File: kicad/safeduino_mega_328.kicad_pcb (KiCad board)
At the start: 2 copper layers, 134.5 x 63.9 mm, 333 parts, among them X1 USB

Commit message: Начал переразводить печатную плату.
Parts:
- removed XSJG1: ~, SIL-4
- added C1: 22п, SMD0805, B.Cu at (68.6, 101.1)
- added C10: 0.1мк, SMD0805, B.Cu at (107.8, 133.0)
- added C8: 0.1мк, SMD0805, B.Cu at (72.3, 119.0)
- added C9: 0.1мк, SMD0805, F.Cu at (69.6, 121.2)
- added R10: 10к, SMD0805, B.Cu at (72.3, 115.1)
- added R11: 1M, SMD0805, B.Cu at (72.9, 101.1)
- added R12: 10к, SMD0805, F.Cu at (82.5, 119.3)
- added R13: 10к, SMD0805, F.Cu at (82.5, 113.5)
- added R14: 1к, SMD0805, B.Cu at (105.5, 133.9)
- added R15: 0, SMD0805, B.Cu at (104.6, 130.8)
- added R16: 1М, SMD0805, B.Cu at (110.1, 133.0)
- added R9: 1к, SMD0805, F.Cu at (58.8, 120.4)
- added VD5: BAS216, SOD110, B.Cu at (69.8, 113.9)
- added XP1: PLD-6, PIN_ARRAY_3x2, F.Cu at (85.1, 104.6)
- added Z2: 16МГц, Q_49U3HMS&, F.Cu at (72.9, 104.5)
- C3: value 0.1мк -> 22п; moved to B.Cu
- C4: moved to B.Cu
- C5: value 0.1мк -> 1мк; moved to B.Cu
- DD2: value FT232RL -> ATMEGA16U2-MU; footprint TSOP28 -> TQFP32_case
- DD3: value ADUM1201 -> ADUM1301; footprint SOIC8 -> SOIC16_RW16
- R3: value 47 -> 22
- R4: value 1к -> 22
- XP2: footprint pin_array_3x2 -> PIN_ARRAY_3x2
- XS1, XS3, XS5, XS6: footprint SIL-8 -> PIN_ARRAY_8x1
- XS2, XS4: footprint SIL-6 -> PIN_ARRAY_6x1
- moved VD4 26.5 mm to (64.1, 120.8), turned to 0 degrees
- moved C5 22.7 mm to (66.3, 114.4)
- moved R4 19.2 mm to (66.2, 110.9), turned to 0 degrees
- moved C2 19.0 mm to (77.5, 128.1), turned to 0 degrees
- moved R3 18.7 mm to (66.2, 108.6)
- moved VD3 17.6 mm to (64.1, 117.9)
- moved C3 11.4 mm to (77.2, 101.1), turned to 0 degrees
- moved R2 11.0 mm to (65.7, 114.3), turned to 90 degrees
- moved C4 8.77 mm to (74.2, 120.5), turned to 0 degrees
- moved C12 7.39 mm to (82.0, 110.4), turned to 0 degrees
- moved DD2 5.53 mm to (74.7, 115.6)
- moved C6 2.44 mm to (75.9, 124.6), turned to 0 degrees
- moved R7 2.08 mm to (98.3, 115.2)
- moved C13 1.73 mm to (93.5, 108.3), turned to 180 degrees
- moved DA1 1.52 mm to (85.5, 123.8)
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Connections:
- C3 pad 1: N-0000013 -> N-0000060
- C4 pad 1: /5V_USB -> /GND_USB
- C4 pad 2: /GND_USB -> /5V_USB
- C5 pad 1: /GND_USB -> N-0000065
- C5 pad 2: /5V_USB -> /GND_USB
- DD2 pad 1: N-0000026 -> N-000003
- DD2 pad 10: /DCD -> /RXI
- DD2 pad 11: /CTS -> /TXI
- DD2 pad 13: (no net) -> /RESET2
- DD2 pad 15: N-0000061 -> /SCK2
- DD2 pad 16: N-0000060 -> /MOSI2
- DD2 pad 17: N-0000013 -> /MISO2
- DD2 pad 18: /GND_USB -> (no net)
- DD2 pad 19: /5V_USB -> (no net)
- DD2 pad 2: (no net) -> N-0000060
- DD2 pad 20: /5V_USB -> (no net)
- DD2 pad 21: /GND_USB -> (no net)
- DD2 pad 22: N-0000032 -> (no net)
- DD2 pad 23: N-0000036 -> (no net)
- DD2 pad 24: (no net) -> /RESET_16U2
- DD2 pad 25: /GND_USB -> (no net)
- DD2 pad 26: /GND_USB -> (no net)
- DD2 pad 27: (no net) -> N-0000065
- DD2 pad 28: (no net) -> /GND_USB
- DD2 pad 3: (no net) -> /GND_USB
- DD2 pad 5: N-0000038 -> (no net)
- DD2 pad 6: /RI -> (no net)
- DD2 pad 7: /GND_USB -> (no net)
- DD2 pad 9: /DSR -> /PE0
- DD3 pad 2: N-0000038 -> /GND_USB
- DD3 pad 3: N-0000064 -> /RESET2
- DD3 pad 4: /GND_USB -> N-0000047
- DD3 pad 5: /GND -> (no net)
- DD3 pad 6: N-0000047 -> (no net)
- DD3 pad 7: N-0000048 -> (no net)
- DD3 pad 8: /MPU_VCC -> /GND_USB
- R3 pad 1: N-0000026 -> N-0000034
- R3 pad 2: N-0000064 -> /D-
- R4 pad 1: N-0000057 -> N-0000058
- R4 pad 2: /5V_USB -> /D+
- R6 pad 1: N-0000047 -> N-0000045
- R7 pad 1: N-0000048 -> N-0000043
- VD3 pad 2: N-0000032 -> /RXI
- VD4 pad 2: N-0000036 -> /TXI
- X1 pad 2: N-0000060 -> N-0000034
- X1 pad 3: N-0000061 -> N-0000058
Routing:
- net /5V_USB: track 99.2 -> 2.81 mm, vias 2 -> 0
- net N-0000011: track 0.00 -> 26.5 mm, vias 0 -> 1
- net /DSR: track 25.6 -> 0.00 mm, vias 1 -> 0
- net /CTS: track 25.1 -> 0.00 mm, vias 1 -> 0
- net /MPU_VCC: track 297.0 -> 319.2 mm
- net /GND_USB: track 26.2 -> 6.25 mm, vias 9 -> 0
- net /RESET_16U2: track 0.00 -> 19.2 mm
- net /DCD: track 19.1 -> 0.00 mm, vias 1 -> 0
- net /MOSI2: track 0.00 -> 16.6 mm, vias 0 -> 1
- net N-0000036: track 15.7 -> 0.00 mm
- net /SCK2: track 0.00 -> 15.6 mm, vias 0 -> 1
- net /RI: track 14.4 -> 0.00 mm, vias 1 -> 0
- net N-0000061: track 13.5 -> 0.00 mm
- net N-0000032: track 11.4 -> 0.00 mm
- net N-0000038: track 9.76 -> 0.00 mm
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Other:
- board text removed: "CTS"
- board text removed: "DCD"
- board text removed: "DSR"
- board text removed: "RI"

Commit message: Закончил разводку платы.
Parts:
- C9: moved to B.Cu
- moved C8 7.81 mm to (64.5, 118.0), turned to 180 degrees
- moved R10 7.47 mm to (67.9, 109.0)
- moved VD5 7.19 mm to (65.7, 108.1)
- moved C4 4.70 mm to (77.9, 123.4), turned to 180 degrees
- moved C9 1.67 mm to (69.8, 122.8)
- moved C2 0.97 mm to (77.9, 127.3), turned to 180 degrees
- moved C6 0.57 mm to (75.7, 124.1), turned to 180 degrees
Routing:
- net /5V_USB: track 2.81 -> 105.5 mm, vias 0 -> 3
- net /GND_USB: track 6.25 -> 60.2 mm, vias 0 -> 5
- net N-000003: track 6.18 -> 27.1 mm, vias 0 -> 1
- net /TXI: track 0.00 -> 20.4 mm, vias 0 -> 2
- net N-0000060: track 6.18 -> 25.8 mm, vias 0 -> 1
- net /D-: track 0.00 -> 17.9 mm, vias 0 -> 2
- net /RXI: track 0.00 -> 14.7 mm, vias 0 -> 2
- net /D+: track 0.00 -> 13.3 mm, vias 0 -> 2
- net /RESET_16U2: track 19.2 -> 29.1 mm, vias 0 -> 1
- net N-0000065: track 0.00 -> 5.87 mm, vias 0 -> 1
- net /GND: track 134.9 -> 138.9 mm
- net /MOSI2: track 16.6 -> 13.6 mm
- net /SCK2: track 15.6 -> 14.2 mm

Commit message: Добавил самовостанавливающиеся предохренители на 0.5А.
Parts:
- added FU1: MF-MSMF050, SMD1812, B.Cu at (62.9, 103.9)
- added FU2: MF-MSMF050, SMD1812, B.Cu at (133.1, 140.1)
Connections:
- VD1 pad 1: N-0000031 -> N-0000057
- X1 pad 1: /5V_USB -> N-0000042
- XP3 pad 1: N-0000031 -> N-0000056
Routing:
- net N-0000042: track 0.00 -> 19.7 mm, vias 0 -> 1
- net N-0000056: track 0.00 -> 10.3 mm
- net N-0000057: track 0.00 -> 7.89 mm, vias 0 -> 1
- net N-0000031: track 6.36 -> 0.00 mm
- net /5V_USB: track 105.5 -> 108.2 mm, vias 3 -> 4

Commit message: Заменил резистор R15 на диод VD6  для защиты ADUM от попадания напряжения.
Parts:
- removed R15: 0, SMD0805
- added VD6: BAS216, SOD110, B.Cu at (103.1, 130.8)
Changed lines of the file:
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@@
     (thickness 1.6002)
     (drawings 81)
-    (tracks 943)
+    (tracks 944)
     (zones 0)
     (modules 349)
@@
   )
   (setup
-    (last_trace_width 0.508)
+    (last_trace_width 0.254)
     (user_trace_width 0.254)
     (user_trace_width 0.508)
@@
     )
   )
-  (module SMD0805 (layer Back)
-    (at 104.648 130.81)
-    (attr smd)
-    (fp_text reference R15 (at 0 -1.524) (layer B.SilkS)
-      (effects (font (size 0.635 0.635) (thickness 0.127)) (justify mirror))
-    )
-    (fp_text value 0 (at 0.254 -1.524) (layer B.SilkS) hide
-      (effects (font (size 0.635 0.635) (thickness 0.127)) (justify mirror))
-    )
-    (fp_line (start 1.778 -1.016) (end 1.778 1.016) (layer B.SilkS) (width 0.127))
-    (fp_line (start -1.778 -1.016) (end 1.778 -1.016) (layer B.SilkS) (width 0.127))
-    (fp_line (start -1.778 1.016) (end -1.778 -1.016) (layer B.SilkS) (width 0.127))
-    (fp_line (start -1.778 1.016) (end 1.778 1.016) (layer B.SilkS) (width 0.127))
-    (pad 1 smd rect (at -0.9525 0) (size 0.889 1.397)
-      (layers Back B.Paste B.Mask)
-      (net 40 N-0000013)
-    )
-    (pad 2 smd rect (at 0.9525 0) (size 0.889 1.397)
-      (layers Back B.Paste B.Mask)
-      (net 48 N-0000055)
-    )
-    (model smd/chip_cms.wrl
-      (at (xyz 0 0 0))
-      (scale (xyz 0.1 0.1 0.1))
-      (rotate (xyz 0 0 0))
-    )
-  )
   (module SMD0805 (layer Front)
     (at 82.042 110.363)
@@
     )
   )
+  (module SOD110 (layer Back)
+    (at 103.124 130.81)
+    (tags SOT23_5)
+    (fp_text reference VD6 (at 1.27 -1.778) (layer B.SilkS)
+      (effects (font (size 0.762 0.762) (thickness 0.0762)) (justify mirror))
+    )
+    (fp_text value BAS216 (at 1.397 -1.778) (layer B.SilkS) hide
+      (effects (font (size 0.762 0.50038) (thickness 0.0762)) (justify mirror))
+    )
+    (fp_line (start -0.889 -1.016) (end 3.556 -1.016) (layer B.SilkS) (width 0.127))
+    (fp_line (start 3.556 1.016) (end -0.889 1.016) (layer B.SilkS) (width 0.127))
+    (fp_line (start 3.556 1.016) (end 3.556 -1.016) (layer B.SilkS) (width 0.127))
+    (fp_line (start -0.889 -1.016) (end -0.889 1.016) (layer B.SilkS) (width 0.127))
+    (fp_line (start 3.302 1.016) (end 3.302 -1.016) (layer B.SilkS) (width 0.127))
+    (pad 2 smd rect (at 2.3495 0) (size 1.00076 1.19888)
+      (layers Back B.Paste B.Mask)
+      (net 48 N-0000055)
+    )
+    (pad 1 smd rect (at 0 0) (size 1.00076 1.19888)
+      (layers Back B.Paste B.Mask)
+      (net 40 N-0000013)
+    )
+    (model smd/SOT23_6.wrl
+      (at (xyz 0 0 0))
+      (scale (xyz 0.11 0.11 0.11))
+      (rotate (xyz 0 0 -180))
+    )
+  )
   (gr_text "SafeDuino MEGA 328 \nrev 1.02" (at 57.277 131.064 90) (layer F.SilkS)
     (effects (font (size 1.09982 1.09982) (thickness 0.17018)))
@@
   (segment (start 85.471 139.065) (end 78.105 139.065) (width 0.508) (layer Front) (net 39))
   (segment (start 78.105 139.065) (end 77.47 139.7) (width 0.508) (layer Front) (net 39))
-  (segment (start 103.6955 130.81) (end 101.6 130.81) (width 0.254) (layer Back) (net 40))
+  (segment (start 101.473 130.683) (end 102.997 130.683) (width 0.254) (layer Back) (net 40) (status 800000))
+  (segment (start 102.997 130.683) (end 103.124 130.81) (width 0.254) (layer Back) (net 40) (status C00000))
   (segment (start 94.107 113.411) (end 95.25 113.411) (width 0.254) (layer Front) (net 40))
   (segment (start 93.345 114.173) (end 94.107 113.411) (width 0.254) (layer Front) (net 40))

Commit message: SafeDuino MEGA 328 v1.02 полностью готова к отправке на изготовление.
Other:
- board text added: "+5V"

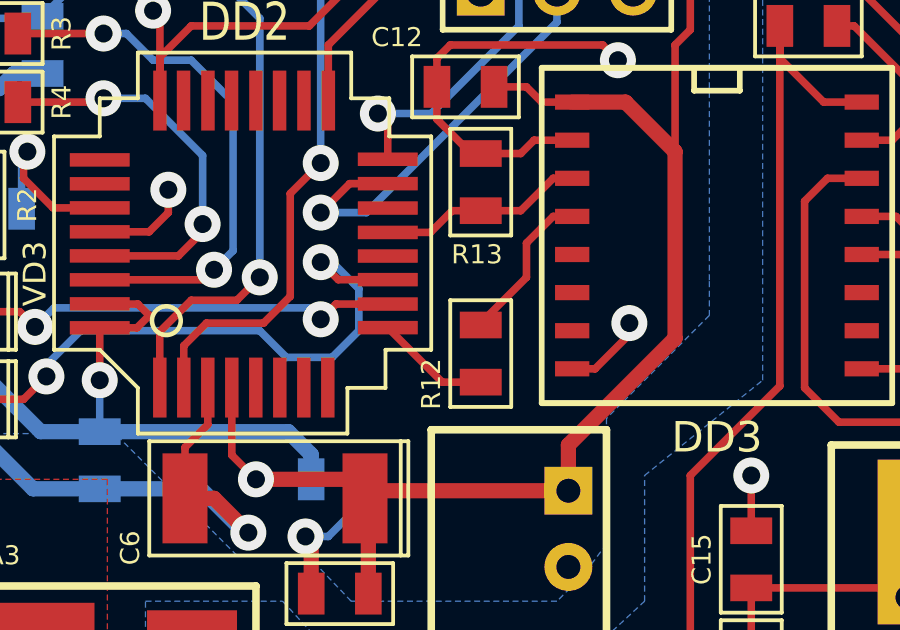
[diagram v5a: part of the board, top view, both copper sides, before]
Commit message: Исправли ошибку на плате SafeDuino MEGA 328(был не соединён контакт PE0 на плате).
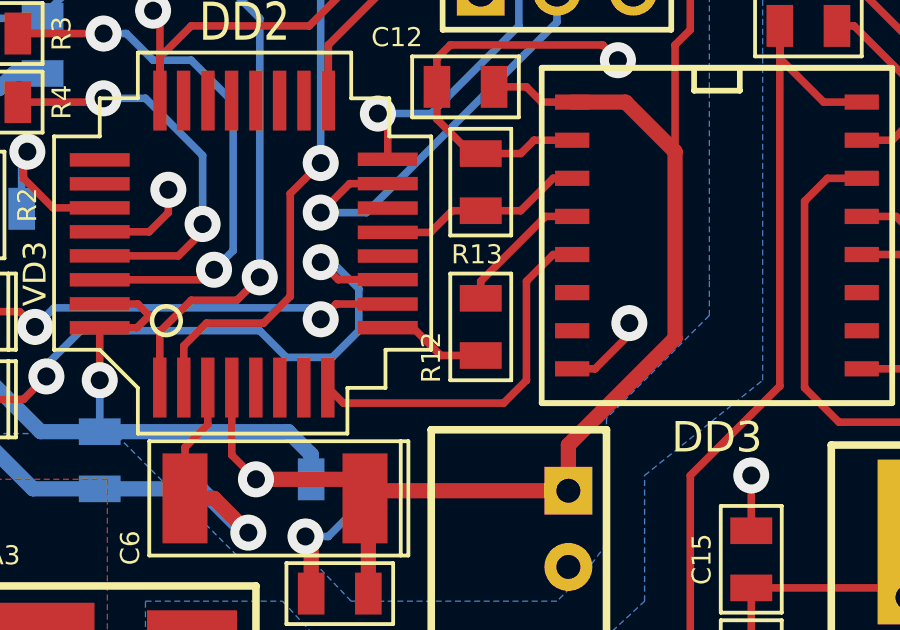
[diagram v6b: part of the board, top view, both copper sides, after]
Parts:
- R12: value 10к -> 47
- R13: value 10к -> 1к
- R16: value 1М -> 1M
- moved R12 0.89 mm to (82.5, 118.4)
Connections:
- DD1 pad 19: (no net) -> Net-(DD1-Pad19)
- DD1 pad 22: (no net) -> Net-(DD1-Pad22)
- DD2 pad 12: (no net) -> Net-(DD2-Pad12)
- DD2 pad 14: (no net) -> Net-(DD2-Pad14)
- DD2 pad 18: (no net) -> Net-(DD2-Pad18)
- DD2 pad 19: (no net) -> Net-(DD2-Pad19)
- DD2 pad 20: (no net) -> Net-(DD2-Pad20)
- DD2 pad 21: (no net) -> Net-(DD2-Pad21)
- DD2 pad 22: (no net) -> Net-(DD2-Pad22)
- DD2 pad 23: (no net) -> Net-(DD2-Pad23)
- DD2 pad 25: (no net) -> Net-(DD2-Pad25)
- DD2 pad 26: (no net) -> Net-(DD2-Pad26)
- DD2 pad 5: (no net) -> Net-(DD2-Pad5)
- DD2 pad 6: (no net) -> Net-(DD2-Pad6)
- DD2 pad 7: (no net) -> Net-(DD2-Pad7)
- DD2 pad 8: (no net) -> /PE1
- DD3 pad 10: (no net) -> Net-(DD3-Pad10)
- DD3 pad 5: (no net) -> /PE1
- DD3 pad 7: (no net) -> Net-(DD3-Pad7)
- X1 pad 5: (no net) -> Net-(X1-Pad5)
- X1 pad 6: (no net) -> Net-(X1-Pad6)
- XP4 pad 10: (no net) -> Net-(XP4-Pad10)
- XP4 pad 7: (no net) -> Net-(XP4-Pad7)
- XP4 pad 8: (no net) -> Net-(XP4-Pad8)
- XP4 pad 9: (no net) -> Net-(XP4-Pad9)
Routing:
- net /PE1: track 0.00 -> 12.3 mm
- net Net-(DD3-Pad4): track 5.25 -> 4.51 mm

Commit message: Поправил шелкографию на плате.
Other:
- board text added: "SafeDuino MEGA 328 rev 1.03"
- board text removed: "SafeDuino MEGA 328 rev 1.02"
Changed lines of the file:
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@@
     (pad_to_mask_clearance 0.254)
     (aux_axis_origin 0 0)
-    (visible_elements FFFFFFBF)
+    (visible_elements FFFFFFFF)
     (pcbplotparams
       (layerselection 0x010f0_80000001)
@@
       (drillshape 0)
       (scaleselection 1)
-      (outputdirectory ../../../../Documents/GERBER_safeduino_mega_328/))
+      (outputdirectory ../../../../Документы/GERBER_safeduino_mega_328/))
   )
   (net 0 "")
@@
     (at 65.659 108.077 270)
     (tags SOT23_5)
-    (fp_text reference VD5 (at -1.524 0 360) (layer B.SilkS)
+    (fp_text reference VD5 (at -1.651 -0.635 360) (layer B.SilkS)
       (effects (font (size 0.762 0.762) (thickness 0.0762)) (justify mirror))
     )
@@
     (at 82.55 118.364 90)
     (attr smd)
-    (fp_text reference R12 (at -1.016 -1.651 90) (layer F.SilkS)
+    (fp_text reference R12 (at -2.54 0 180) (layer F.SilkS)
       (effects (font (size 0.635 0.635) (thickness 0.127)))
     )
@@
     (at 67.945 108.966 270)
     (attr smd)
-    (fp_text reference R10 (at -2.413 0 360) (layer B.SilkS)
+    (fp_text reference R10 (at -2.286 -0.889 360) (layer B.SilkS)
       (effects (font (size 0.635 0.635) (thickness 0.127)) (justify mirror))
     )
@@
     (at 64.516 117.983 180)
     (attr smd)
-    (fp_text reference C8 (at -2.54 0 270) (layer B.SilkS)
+    (fp_text reference C8 (at 2.54 0.127 270) (layer B.SilkS)
       (effects (font (size 0.635 0.635) (thickness 0.127)) (justify mirror))
     )
@@
     (effects (font (size 1.016 1.016) (thickness 0.2032)))
   )
-  (gr_text "SafeDuino MEGA 328 \nrev 1.02" (at 57.277 131.064 90) (layer F.SilkS)
+  (gr_text "SafeDuino MEGA 328 \nrev 1.03" (at 57.277 131.064 90) (layer F.SilkS)
     (effects (font (size 1.09982 1.09982) (thickness 0.17018)))
   )
@@
   (segment (start 110.998 108.712) (end 111.4552 109.1692) (width 0.254) (layer Front) (net 25))
   (segment (start 99.187 94.107) (end 99.187 96.647) (width 0.254) (layer Back) (net 25) (status C00))
-  (segment (start 79.4512 118.3894) (end 80.2894 118.3894) (width 0.254) (layer Front) (net 26) (status C00000))
-  (segment (start 80.2894 118.3894) (end 81.2165 119.3165) (width 0.254) (layer Front) (net 26) (status 400000))
-  (segment (start 81.2165 119.3165) (end 82.55 119.3165) (width 0.254) (layer Front) (net 26) (status 800000))
+  (segment (start 79.4512 118.3894) (end 80.2894 118.3894) (width 0.254) (layer Front) (net 26))
+  (segment (start 80.2894 118.3894) (end 81.2165 119.3165) (width 0.254) (layer Front) (net 26))
+  (segment (start 81.2165 119.3165) (end 82.55 119.3165) (width 0.254) (layer Front) (net 26))
   (segment (start 107.823 133.9215) (end 110.109 133.9215) (width 0.254) (layer Back) (net 27))
   (segment (start 110.109 133.9215) (end 110.109 134.239) (width 0.254) (layer Back) (net 27))
@@
   (segment (start 96.4565 127.0635) (end 96.774 127.381) (width 0.254) (layer Front) (net 45))
   (segment (start 91.567 128.9685) (end 91.567 127.0635) (width 0.254) (layer Front) (net 45) (status C00))
-  (segment (start 85.598 115.951) (end 84.963 115.951) (width 0.254) (layer Front) (net 48) (status 400000))
-  (segment (start 77.97038 120.904) (end 77.45222 120.38584) (width 0.254) (layer Front) (net 48) (status 800000))
+  (segment (start 85.598 115.951) (end 84.963 115.951) (width 0.254) (layer Front) (net 48))
+  (segment (start 77.97038 120.904) (end 77.45222 120.38584) (width 0.254) (layer Front) (net 48))
   (segment (start 83.312 120.904) (end 77.97038 120.904) (width 0.254) (layer Front) (net 48))
   (segment (start 84.074 120.142) (end 83.312 120.904) (width 0.254) (layer Front) (net 48))
@@
   (segment (start 96.8375 116.1415) (end 98.298 116.1415) (width 0.254) (layer Front) (net 64))
   (segment (start 96.647 115.951) (end 96.8375 116.1415) (width 0.254) (layer Front) (net 64))
-  (segment (start 82.55 117.4115) (end 82.55 116.84) (width 0.254) (layer Front) (net 67) (status 400000))
+  (segment (start 82.55 117.4115) (end 82.55 116.84) (width 0.254) (layer Front) (net 67))
   (segment (start 82.55 116.84) (end 84.709 114.681) (width 0.254) (layer Front) (net 67))
-  (segment (start 84.709 114.681) (end 85.598 114.681) (width 0.254) (layer Front) (net 67) (status 800000))
+  (segment (start 84.709 114.681) (end 85.598 114.681) (width 0.254) (layer Front) (net 67))
   (segment (start 59.944 105.41) (end 57.785 107.569) (width 0.508) (layer Front) (net 68))
   (segment (start 61.087 104.267) (end 62.611 104.267) (width 0.508) (layer Front) (net 68))
